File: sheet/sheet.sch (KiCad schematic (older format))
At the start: 65 parts

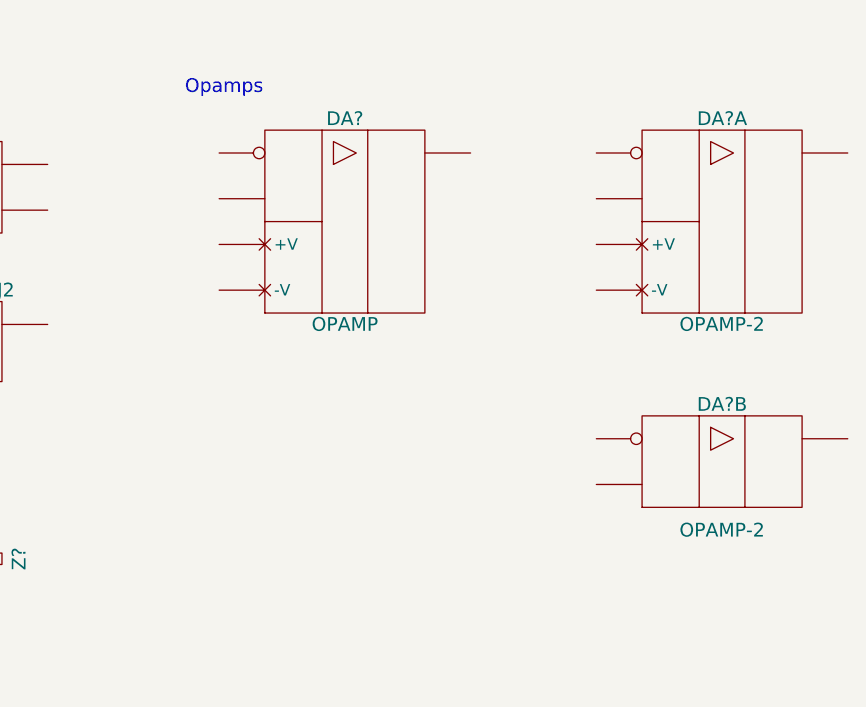
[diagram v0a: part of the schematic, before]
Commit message: Revise opamps
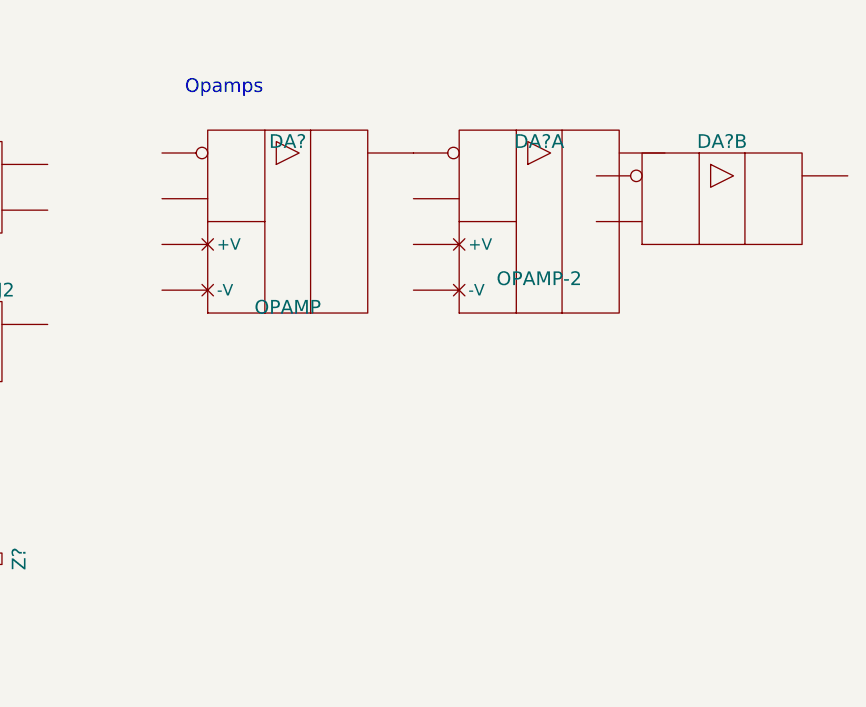
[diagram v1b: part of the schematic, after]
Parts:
- removed DA?: OPAMP, symbol OPAMP
- removed DA? (x2): OPAMP-2, symbol OPAMP-2
- added DA? (x2): OPAMP-2, symbol OPAMP-2
- added DA?: OPAMP, symbol OPAMP
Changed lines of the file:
@@
 Text Notes 5700 2500 0    60   ~ 0
 Other
-$Comp
-L OPAMP DA?
-U 1 1 55D9D5E8
-P 8450 1300
-F 0 "DA?" H 8450 1750 60  0000 C CNN
-F 1 "OPAMP" H 8450 850 60  0000 C CNN
-F 2 "" H 8450 1100 60  0000 C CNN
-F 3 "" H 8450 1100 60  0000 C CNN
-	1    8450 1300
-	1    0    0    -1
-$EndComp
-$Comp
-L OPAMP-2 DA?
-U 1 1 55D9D68F
-P 10100 1300
-F 0 "DA?" H 10100 1750 60  0000 C CNN
-F 1 "OPAMP-2" H 10100 850 60  0000 C CNN
-F 2 "" H 10100 1050 60  0000 C CNN
-F 3 "" H 10100 1050 60  0000 C CNN
-	1    10100 1300
-	1    0    0    -1
-$EndComp
-$Comp
-L OPAMP-2 DA?
-U 2 1 55D9DBC8
-P 10100 2350
-F 0 "DA?" H 10100 2600 60  0000 C CNN
-F 1 "OPAMP-2" H 10100 2050 60  0000 C CNN
-F 2 "" H 10100 2100 60  0000 C CNN
-F 3 "" H 10100 2100 60  0000 C CNN
-	2    10100 2350
-	1    0    0    -1
-$EndComp
 Text Notes 7750 750  0    60   ~ 0
 Opamps
@@
 	1    0    0    -1
 $EndComp
+$Comp
+L OPAMP-2 DA?
+U 1 1 560E69E5
+P 9300 1300
+F 0 "DA?" H 9300 1650 60  0000 C CNN
+F 1 "OPAMP-2" H 9300 1050 60  0000 C CNN
+F 2 "" H 9200 950 60  0000 C CNN
+F 3 "" H 9200 950 60  0000 C CNN
+	1    9300 1300
+	1    0    0    -1
+$EndComp
+$Comp
+L OPAMP-2 DA?
+U 2 1 560E6C00
+P 10100 1200
+F 0 "DA?" H 10100 1450 60  0000 C CNN
+F 1 "OPAMP-2" H 10100 950 60  0001 C CNN
+F 2 "" H 10000 850 60  0000 C CNN
+F 3 "" H 10000 850 60  0000 C CNN
+	2    10100 1200
+	1    0    0    -1
+$EndComp
+$Comp
+L OPAMP DA?
+U 1 1 560E7133
+P 8200 1300
+F 0 "DA?" H 8200 1650 60  0000 C CNN
+F 1 "OPAMP" H 8200 925 60  0000 C CNN
+F 2 "" H 8200 1000 60  0000 C CNN
+F 3 "" H 8200 1000 60  0000 C CNN
+	1    8200 1300
+	1    0    0    -1
+$EndComp

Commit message: Add rheostat type variable resistor. Fix trim resistor.
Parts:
- added R?: R_Var_Rheostat, symbol R_Var_Rheostat
- added R?: R_0,05W, symbol R_0,05W
- added R?: R_0,25W, symbol R_0,25W
- added R?: R_0,5W, symbol R_0,5W
- added R?: R_1W, symbol R_1W
- added R?: R_2W, symbol R_2W
- added R?: R_5W, symbol R_5W
- added R?: R_NON_LINEAR, symbol R_NON_LINEAR
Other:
- moved on the sheet: R?
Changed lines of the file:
@@
 EESchema Schematic File Version 2
-LIBS:connectors
-LIBS:indicators
-LIBS:opamps
-LIBS:other
 LIBS:power
-LIBS:regulators
-LIBS:rlc
-LIBS:semiconductors
-LIBS:switches
-LIBS:sheet-cache
+LIBS:generic
 EELAYER 25 0
 EELAYER END
@@
 L Fuse FU?
 U 1 1 55D8CAF1
-P 1650 2050
-F 0 "FU?" H 1650 2150 50  0000 C CNN
-F 1 "Fuse" H 1650 1950 50  0000 C CNN
-F 2 "" H 1700 1850 60  0000 C CNN
-F 3 "" H 1650 2050 60  0000 C CNN
-	1    1650 2050
+P 1050 2100
+F 0 "FU?" H 1050 2200 50  0000 C CNN
+F 1 "Fuse" H 1050 2000 50  0000 C CNN
+F 2 "" H 1100 1900 60  0000 C CNN
+F 3 "" H 1050 2100 60  0000 C CNN
+	1    1050 2100
 	1    0    0    -1
 $EndComp
@@
 L R R?
 U 1 1 55D8CB70
-P 1650 2550
-F 0 "R?" V 1755 2550 50  0000 C CNN
-F 1 "R" V 1550 2550 50  0000 C CNN
-F 2 "" H 1650 2550 60  0000 C CNN
-F 3 "" H 1650 2550 60  0000 C CNN
-	1    1650 2550
-	0    1    1    0
+P 2850 2200
+F 0 "R?" V 2955 2200 50  0000 C CNN
+F 1 "R" V 2750 2200 50  0000 C CNN
+F 2 "" H 2850 2200 60  0000 C CNN
+F 3 "" H 2850 2200 60  0000 C CNN
+	1    2850 2200
+	1    0    0    -1
 $EndComp
 $Comp
@@
 L Polyfuse FU?
 U 1 1 55D8CD66
-P 1050 2050
-F 0 "FU?" H 1055 2200 50  0000 C CNN
-F 1 "Polyfuse" H 1050 1850 50  0000 C CNN
-F 2 "" H 1050 2050 60  0000 C CNN
-F 3 "" H 1050 2050 60  0000 C CNN
-	1    1050 2050
+P 1650 2100
+F 0 "FU?" H 1655 2250 50  0000 C CNN
+F 1 "Polyfuse" H 1650 1900 50  0000 C CNN
+F 2 "" H 1650 2100 60  0000 C CNN
+F 3 "" H 1650 2100 60  0000 C CNN
+	1    1650 2100
 	1    0    0    -1
 $EndComp
@@
 L R_0,125W R?
 U 1 1 55DBA828
-P 2250 2050
-F 0 "R?" V 2355 2050 50  0000 C CNN
-F 1 "R_0,125W" V 2150 2050 50  0000 C CNN
-F 2 "" H 2250 2050 60  0000 C CNN
-F 3 "" H 2250 2050 60  0000 C CNN
-	1    2250 2050
-	0    1    1    0
+P 3650 2200
+F 0 "R?" V 3755 2200 50  0000 C CNN
+F 1 "R_0,125W" V 3550 2200 50  0000 C CNN
+F 2 "" H 3650 2200 60  0000 C CNN
+F 3 "" H 3650 2200 60  0000 C CNN
+	1    3650 2200
+	-1   0    0    1
 $EndComp
 $Comp
@@
 	1    0    0    -1
 $EndComp
+$Comp
+L R_Var_Rheostat R?
+U 1 1 56A0BA19
+P 2250 3050
+F 0 "R?" H 2255 3200 50  0000 C CNN
+F 1 "R_Var_Rheostat" H 2250 2900 50  0000 C CNN
+F 2 "" H 2250 3050 60  0000 C CNN
+F 3 "" H 2250 3050 60  0000 C CNN
+	1    2250 3050
+	1    0    0    -1
+$EndComp
+$Comp
+L R_0,05W R?
+U 1 1 56A0C7EE
+P 3250 2200
+F 0 "R?" V 3355 2200 50  0000 C CNN
+F 1 "R_0,05W" V 3150 2200 50  0000 C CNN
+F 2 "" H 3250 2200 60  0000 C CNN
+F 3 "" H 3250 2200 60  0000 C CNN
+	1    3250 2200
+	-1   0    0    1
+$EndComp
+$Comp
+L R_0,25W R?
+U 1 1 56A0C88F
+P 4100 2200
+F 0 "R?" V 4205 2200 50  0000 C CNN
+F 1 "R_0,25W" V 4000 2200 50  0000 C CNN
+F 2 "" H 4100 2200 60  0000 C CNN
+F 3 "" H 4100 2200 60  0000 C CNN
+	1    4100 2200
+	1    0    0    -1
+$EndComp
+$Comp
+L R_0,5W R?
+U 1 1 56A11D4B
+P 2850 2800
+F 0 "R?" V 2955 2800 50  0000 C CNN
+F 1 "R_0,5W" V 2750 2800 50  0000 C CNN
+F 2 "" H 2850 2800 60  0000 C CNN
+F 3 "" H 2850 2800 60  0000 C CNN
+	1    2850 2800
+	1    0    0    -1
+$EndComp
+$Comp
+L R_1W R?
+U 1 1 56A11E53
+P 3250 2800
+F 0 "R?" V 3355 2800 50  0000 C CNN
+F 1 "R_1W" V 3150 2800 50  0000 C CNN
+F 2 "" H 3250 2800 60  0000 C CNN
+F 3 "" H 3250 2800 60  0000 C CNN
+	1    3250 2800
+	1    0    0    -1
+$EndComp
+$Comp
+L R_2W R?
+U 1 1 56A13D48
+P 3650 2800
+F 0 "R?" V 3755 2800 50  0000 C CNN
+F 1 "R_2W" V 3550 2800 50  0000 C CNN
+F 2 "" H 3650 2800 60  0000 C CNN
+F 3 "" H 3650 2800 60  0000 C CNN
+	1    3650 2800
+	1    0    0    -1
+$EndComp
+$Comp
+L R_5W R?
+U 1 1 56A13E8C
+P 4100 2800
+F 0 "R?" V 4205 2800 50  0000 C CNN
+F 1 "R_5W" V 4000 2800 50  0000 C CNN
+F 2 "" H 4100 2800 60  0000 C CNN
+F 3 "" H 4100 2800 60  0000 C CNN
+	1    4100 2800
+	1    0    0    -1
+$EndComp
+$Comp
+L R_NON_LINEAR R?
+U 1 1 56A18CBD
+P 1650 2550
+F 0 "R?" H 1655 2700 50  0000 C CNN
+F 1 "R_NON_LINEAR" H 1650 2375 50  0000 C CNN
+F 2 "" H 1650 2550 60  0000 C CNN
+F 3 "" H 1650 2550 60  0000 C CNN
+	1    1650 2550
+	1    0    0    -1
+$EndComp

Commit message: Add schmitt trigger, relay, some switches
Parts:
- added DD? (x2): Schmitt_Trigger, symbol Schmitt_Trigger
- added DD? (x2): Schmitt_Trigger_2, symbol Schmitt_Trigger_2
- added SA?: Switch, symbol Switch
- added SA?: Switch_Changeover, symbol Switch_Changeover
- added SA?: Switch_NC, symbol Switch_NC
- added SA? (x2): Relay_Changeover, symbol Relay_Changeover
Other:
- moved on the sheet: C?, DA?, DA?A, DA?B, HL?, L?, R?, S?, SB?, VT?, XP?, XS?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

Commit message: Add dual gate n mosfet
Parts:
- added VT?: NMOSFET_Dual_Gate, symbol NMOSFET_Dual_Gate
- added VT?: NMOSFET_Dual_Gate_DE, symbol NMOSFET_Dual_Gate_DE
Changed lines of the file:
@@
 	0    -1   -1   0
 $EndComp
+$Comp
+L NMOSFET_Dual_Gate VT?
+U 1 1 57385B8C
+P 1500 8350
+F 0 "VT?" H 1575 8225 60  0000 R CNN
+F 1 "NMOSFET_Dual_Gate" H 1500 8525 60  0000 C CNN
+F 2 "" H 1450 8375 60  0000 C CNN
+F 3 "" H 1450 8375 60  0000 C CNN
+	1    1500 8350
+	1    0    0    -1
+$EndComp
+$Comp
+L NMOSFET_Dual_Gate_DE VT?
+U 1 1 5738C11C
+P 1500 8800
+F 0 "VT?" H 1575 8675 60  0000 R CNN
+F 1 "NMOSFET_Dual_Gate_DE" H 1500 8975 60  0000 C CNN
+F 2 "" H 1450 8825 60  0000 C CNN
+F 3 "" H 1450 8825 60  0000 C CNN
+	1    1500 8800
+	1    0    0    -1
+$EndComp
 $EndSCHEMATC

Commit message: Coax connector, various corrections
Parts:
- added XW?: CONN_COAX_F, symbol CONN_COAX_F
- added XW?: CONN_COAX_M, symbol CONN_COAX_M
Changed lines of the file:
@@
+	1    0    0    -1
+$EndComp
+$Comp
+L CONN_COAX_F XW?
+U 1 1 5914D377
+P 6450 5850
+F 0 "XW?" H 6600 6000 60  0000 C CNN
+F 1 "CONN_COAX_F" H 6600 5700 60  0001 C CNN
+F 2 "" H 6450 5850 60  0000 C CNN
+F 3 "" H 6450 5850 60  0000 C CNN
+	1    6450 5850
+	1    0    0    -1
+$EndComp
+$Comp
+L CONN_COAX_M XW?
+U 1 1 5914D837
+P 6450 6150
+F 0 "XW?" H 6600 6300 60  0000 C CNN
+F 1 "CONN_COAX_M" H 6600 6000 60  0001 C CNN
+F 2 "" H 6450 6150 60  0000 C CNN
+F 3 "" H 6450 6150 60  0000 C CNN
+	1    6450 6150
 	1    0    0    -1
 $EndComp

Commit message: refactor: KiCAD 5 upgrade
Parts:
- C?: symbol C -> Generic_ESKD:C
- C?: symbol C_EL -> Generic_ESKD:C_EL
- C?: symbol C_Pol -> Generic_ESKD:C_Pol
- C?: symbol C_EL_Nonpol -> Generic_ESKD:C_EL_Nonpol
- C?: symbol C_Var -> Generic_ESKD:C_Var
- C?: symbol C_Trim -> Generic_ESKD:C_Trim
- DA?: symbol REG -> Generic_ESKD:REG
- DA?: symbol REG2 -> Generic_ESKD:REG2
- DA?: symbol REG_ADJ -> Generic_ESKD:REG_ADJ
- DA?: symbol REG_ADJ2 -> Generic_ESKD:REG_ADJ2
- DA? (x2): symbol OPAMP-2 -> Generic_ESKD:OPAMP-2
- DA?: symbol OPAMP -> Generic_ESKD:OPAMP
- DD? (x2): symbol Schmitt_Trigger -> Generic_ESKD:Schmitt_Trigger
- DD? (x2): symbol Schmitt_Trigger_2 -> Generic_ESKD:Schmitt_Trigger_2
- FU?: symbol Fuse -> Generic_ESKD:Fuse
- FU?: symbol Polyfuse -> Generic_ESKD:Polyfuse
- GB?: symbol Battery -> Generic_ESKD:Battery
- GB?: symbol Battery2 -> Generic_ESKD:Battery2
- HL?: symbol LED -> Generic_ESKD:LED
- L?: symbol L -> Generic_ESKD:L
- L?: symbol L3_Ferrite -> Generic_ESKD:L3_Ferrite
- L?: symbol L_Ferrite -> Generic_ESKD:L_Ferrite
- L?: symbol L3 -> Generic_ESKD:L3
- R?: symbol R -> Generic_ESKD:R
- R?: symbol R_Trim -> Generic_ESKD:R_Trim
- R?: symbol R_Var -> Generic_ESKD:R_Var
- R?: symbol R_0,125W -> Generic_ESKD:R_0,125W
- R?: symbol R_Var_Rheostat -> Generic_ESKD:R_Var_Rheostat
- R?: symbol R_0,05W -> Generic_ESKD:R_0,05W
- R?: symbol R_0,25W -> Generic_ESKD:R_0,25W
- R?: symbol R_0,5W -> Generic_ESKD:R_0,5W
- R?: symbol R_1W -> Generic_ESKD:R_1W
- R?: symbol R_2W -> Generic_ESKD:R_2W
- R?: symbol R_5W -> Generic_ESKD:R_5W
- R?: symbol R_NON_LINEAR -> Generic_ESKD:R_NON_LINEAR
- RK?: symbol Thermistor -> Generic_ESKD:Thermistor
- S?: symbol Jumper -> Generic_ESKD:Jumper
- S?: symbol Jumper3 -> Generic_ESKD:Jumper3
- SA?: symbol Switch -> Generic_ESKD:Switch
- SA?: symbol Switch_Changeover -> Generic_ESKD:Switch_Changeover
- SA?: symbol Switch_NC -> Generic_ESKD:Switch_NC
- SA? (x2): symbol Relay_Changeover -> Generic_ESKD:Relay_Changeover
- SB?: symbol Button2 -> Generic_ESKD:Button2
- SB?: symbol Button -> Generic_ESKD:Button
- VD?: symbol Diode -> Generic_ESKD:Diode
- VD?: symbol Schottky_Diode -> Generic_ESKD:Schottky_Diode
- VD?: symbol Zener_Diode -> Generic_ESKD:Zener_Diode
- VD?: symbol Zener_Diode_Double-anode -> Generic_ESKD:Zener_Diode_Double-anode
- VD?: symbol Varicap -> Generic_ESKD:Varicap
- VD?: symbol Tunnel_Diode -> Generic_ESKD:Tunnel_Diode
- VD?: symbol Backward_Diode -> Generic_ESKD:Backward_Diode
- VD?: symbol Diode_Bridge -> Generic_ESKD:Diode_Bridge
- VD?: symbol Photo_Diode -> Generic_ESKD:Photo_Diode
- VS?: symbol DIAC -> Generic_ESKD:DIAC
- VS?: symbol Dynistor -> Generic_ESKD:Dynistor
- VS?: symbol TRIAC -> Generic_ESKD:TRIAC
- VS?: symbol Thyristor_Anode -> Generic_ESKD:Thyristor_Anode
- VS?: symbol Thyristor_Cathode -> Generic_ESKD:Thyristor_Cathode
- VT?: symbol NPN -> Generic_ESKD:NPN
- VT?: symbol PNP -> Generic_ESKD:PNP
- VT?: symbol NPN_Circle -> Generic_ESKD:NPN_Circle
- VT?: symbol PNP_Circle -> Generic_ESKD:PNP_Circle
- VT?: symbol NJFET_Circle -> Generic_ESKD:NJFET_Circle
- VT?: symbol NJFET -> Generic_ESKD:NJFET
- VT?: symbol PJFET_Circle -> Generic_ESKD:PJFET_Circle
- VT?: symbol PJFET -> Generic_ESKD:PJFET
- VT?: symbol NMOSFET -> Generic_ESKD:NMOSFET
- VT?: symbol NMOSFET_Circle -> Generic_ESKD:NMOSFET_Circle
- VT?: symbol PMOSFET -> Generic_ESKD:PMOSFET
- VT?: symbol PMOSFET_Circle -> Generic_ESKD:PMOSFET_Circle
- VT?: symbol PMOSFET_DE -> Generic_ESKD:PMOSFET_DE
- VT?: symbol PMOSFET_DE_Circle -> Generic_ESKD:PMOSFET_DE_Circle
- VT?: symbol NMOSFET_DE -> Generic_ESKD:NMOSFET_DE
- VT?: symbol NMOSFET_DE_Circle -> Generic_ESKD:NMOSFET_DE_Circle
- VT?: symbol NMOSFET_Dual_Gate -> Generic_ESKD:NMOSFET_Dual_Gate
- VT?: symbol NMOSFET_Dual_Gate_DE -> Generic_ESKD:NMOSFET_Dual_Gate_DE
- XP?: symbol CONN_02_M -> Generic_ESKD:CONN_02_M
- XS?: symbol CONN_02_F -> Generic_ESKD:CONN_02_F
- XS?: symbol PAD -> Generic_ESKD:PAD
- XW?: symbol CONN_COAX_F -> Generic_ESKD:CONN_COAX_F
- XW?: symbol CONN_COAX_M -> Generic_ESKD:CONN_COAX_M
- Z?: symbol Crystal -> Generic_ESKD:Crystal

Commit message: feat: nixie and neon
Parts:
- added HL?: Neon, symbol Generic_ESKD:Neon
- added HL?: Nixie, symbol Generic_ESKD:Nixie
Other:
- moved on the sheet: HL?, XP?, XS?
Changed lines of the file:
@@
 Text Notes 8300 1050 0    60   ~ 0
 Opamps
-Text Notes 5600 4650 0    60   ~ 0
+Text Notes 8500 4500 0    60   ~ 0
 Indicators
 $Comp
 L Generic_ESKD:CONN_02_F XS?
 U 1 1 55DA0C94
-P 6450 5000
-F 0 "XS?" H 6700 5100 60  0000 C CNN
-F 1 "CONN_02_F" H 6800 4800 60  0001 C CNN
-F 2 "" H 6450 5000 60  0000 C CNN
-F 3 "" H 6450 5000 60  0000 C CNN
-	1    6450 5000
+P 6450 4850
+F 0 "XS?" H 6700 4950 60  0000 C CNN
+F 1 "CONN_02_F" H 6800 4650 60  0001 C CNN
+F 2 "" H 6450 4850 60  0000 C CNN
+F 3 "" H 6450 4850 60  0000 C CNN
+	1    6450 4850
 	1    0    0    -1
 $EndComp
@@
 L Generic_ESKD:CONN_02_M XP?
 U 1 1 55DA0E2F
-P 7250 5000
-F 0 "XP?" H 7500 5100 60  0000 C CNN
-F 1 "CONN_02_M" H 7600 4800 60  0001 C CNN
-F 2 "" H 7250 5000 60  0000 C CNN
-F 3 "" H 7250 5000 60  0000 C CNN
-	1    7250 5000
-	1    0    0    -1
-$EndComp
-Text Notes 6450 4650 0    60   ~ 0
+P 7250 4850
+F 0 "XP?" H 7500 4950 60  0000 C CNN
+F 1 "CONN_02_M" H 7600 4650 60  0001 C CNN
+F 2 "" H 7250 4850 60  0000 C CNN
+F 3 "" H 7250 4850 60  0000 C CNN
+	1    7250 4850
+	1    0    0    -1
+$EndComp
+Text Notes 6450 4500 0    60   ~ 0
 Connectors
 $Comp
 L Generic_ESKD:PAD XS?
 U 1 1 55DA139F
-P 6450 5450
-F 0 "XS?" H 6700 5550 60  0000 C CNN
-F 1 "PAD" H 6700 5350 60  0000 C CNN
-F 2 "" H 6450 5450 60  0000 C CNN
-F 3 "" H 6450 5450 60  0000 C CNN
-	1    6450 5450
+P 6450 5300
+F 0 "XS?" H 6700 5400 60  0000 C CNN
+F 1 "PAD" H 6700 5200 60  0000 C CNN
+F 2 "" H 6450 5300 60  0000 C CNN
+F 3 "" H 6450 5300 60  0000 C CNN
+	1    6450 5300
 	1    0    0    -1
 $EndComp
@@
 L Generic_ESKD:LED HL?
 U 1 1 55E52D5F
+P 8600 4850
+F 0 "HL?" H 8600 4725 60  0000 C CNN
+F 1 "LED" H 8600 5100 60  0000 C CNN
+F 2 "" H 8600 4850 60  0000 C CNN
+F 3 "" H 8600 4850 60  0000 C CNN
+	1    8600 4850
+	1    0    0    -1
+$EndComp
+$Comp
+L Generic_ESKD:Photo_Diode VD?
+U 1 1 55E53C55
 P 4300 4850
-F 0 "HL?" H 4300 4725 60  0000 C CNN
-F 1 "LED" H 4300 5100 60  0000 C CNN
+F 0 "VD?" H 4300 4725 60  0000 C CNN
+F 1 "Photo_Diode" H 4300 5125 60  0000 C CNN
 F 2 "" H 4300 4850 60  0000 C CNN
 F 3 "" H 4300 4850 60  0000 C CNN
 	1    4300 4850
-	1    0    0    -1
-$EndComp
-$Comp
-L Generic_ESKD:Photo_Diode VD?
-U 1 1 55E53C55
-P 4950 4850
-F 0 "VD?" H 4950 4725 60  0000 C CNN
-F 1 "Photo_Diode" H 4950 5125 60  0000 C CNN
-F 2 "" H 4950 4850 60  0000 C CNN
-F 3 "" H 4950 4850 60  0000 C CNN
-	1    4950 4850
 	1    0    0    -1
 $EndComp
@@
 L Generic_ESKD:CONN_COAX_F XW?
 U 1 1 5914D377
-P 6450 5850
-F 0 "XW?" H 6600 6000 60  0000 C CNN
-F 1 "CONN_COAX_F" H 6600 5700 60  0001 C CNN
-F 2 "" H 6450 5850 60  0000 C CNN
-F 3 "" H 6450 5850 60  0000 C CNN
-	1    6450 5850
+P 6450 5700
+F 0 "XW?" H 6600 5850 60  0000 C CNN
+F 1 "CONN_COAX_F" H 6600 5550 60  0001 C CNN
+F 2 "" H 6450 5700 60  0000 C CNN
+F 3 "" H 6450 5700 60  0000 C CNN
+	1    6450 5700
 	1    0    0    -1
 $EndComp
@@
 L Generic_ESKD:CONN_COAX_M XW?
 U 1 1 5914D837
-P 6450 6150
-F 0 "XW?" H 6600 6300 60  0000 C CNN
-F 1 "CONN_COAX_M" H 6600 6000 60  0001 C CNN
-F 2 "" H 6450 6150 60  0000 C CNN
-F 3 "" H 6450 6150 60  0000 C CNN
-	1    6450 6150
-	1    0    0    -1
-$EndComp
+P 6450 6000
+F 0 "XW?" H 6600 6150 60  0000 C CNN
+F 1 "CONN_COAX_M" H 6600 5850 60  0001 C CNN
+F 2 "" H 6450 6000 60  0000 C CNN
+F 3 "" H 6450 6000 60  0000 C CNN
+	1    6450 6000
+	1    0    0    -1
+$EndComp
+$Comp
+L Generic_ESKD:Neon HL?
+U 1 1 5C07CF10
+P 8600 5350
+F 0 "HL?" H 8778 5396 50  0000 L CNN
+F 1 "Neon" H 8778 5305 50  0000 L CNN
+F 2 "" H 7700 5350 60  0000 C CNN
+F 3 "" H 7700 5350 60  0000 C CNN
+	1    8600 5350
+	1    0    0    -1
+$EndComp
+$Comp
+L Generic_ESKD:Nixie HL?
+U 1 1 5C07D0C6
+P 10450 5350
+F 0 "HL?" H 9273 5396 50  0000 R CNN
+F 1 "Nixie" H 9273 5305 50  0000 R CNN
+F 2 "" H 9550 5350 60  0000 C CNN
+F 3 "" H 9550 5350 60  0000 C CNN
+	1    10450 5350
+	1    0    0    -1
+$EndComp

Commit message: feat: add npn optocouple
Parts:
- added VT?: Opto_NPN, symbol Generic_ESKD:Opto_NPN
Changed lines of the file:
@@
+	1    0    0    -1
+$EndComp
+$Comp
+L Generic_ESKD:Opto_NPN VT?
+U 1 1 5C74417A
+P 4200 6250
+F 0 "VT?" H 4341 6303 60  0000 L CNN
+F 1 "Opto_NPN" H 4341 6197 60  0000 L CNN
+F 2 "" H 4200 6250 60  0000 C CNN
+F 3 "" H 4200 6250 60  0000 C CNN
+	1    4200 6250
 	1    0    0    -1
 $EndComp
